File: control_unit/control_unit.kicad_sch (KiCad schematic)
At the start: 52 parts, among them J1 Conn_01x02_Pin, J2 Conn_01x02_Pin, J3 Conn_01x04_Pin, J4 Conn_01x04_Pin, J5 BLDC1, J6 Conn_01x04_Pin, J7 BLDC2, J8 BLDC3, J9 BLDC4, Q2 2N7002, U4 BNO055

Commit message: DCDCコンバーター設計開始
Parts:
- removed C10, C3, C7, C8, C9: 22uF, Capacitor_SMD:C_1206_3216Metric, symbol Device:C
- removed C2, C4: 0.1u, symbol Device:C
- removed C5: 1u, symbol Device:C
- removed J2: Conn_01x02_Pin, Connector_PinHeader_2.54mm:PinHeader_1x02_P2.54mm_Vertical, symbol Connector:Conn_01x02_Pin
- removed J3, J6: Conn_01x04_Pin, Connector_PinHeader_2.54mm:PinHeader_1x04_P2.54mm_Vertical, symbol Connector:Conn_01x04_Pin
- removed Q3: ~, Package_TO_SOT_SMD:TO-252-2, symbol basic_parts:MTP7D0N6RJ3
- removed R14: 100k, symbol Device:R
- removed U14: ~, ProLib_pcs_2025-03-30:VSON-10_L3.0-W3.0-P0.50-BR-EP, symbol basic_parts:TPS40303DRCT
- removed U4: BNO055, Package_LGA:LGA-28_5.2x3.8mm_P0.5mm, symbol Sensor_Motion:BNO055
- added Cbst, Cc1, Cc2, Cc3, Css, Cvcc: C, symbol Device:C
- added Cin1, Cin2, Cin3, Cin4, Cin5, Cout1, Cout2, Cout3, Cout4, Cout5, Cout6: 22u, symbol Device:C
- added L2: 6.8uH, symbol Device:L
- added Q2: ~, Package_TO_SOT_SMD:TO-252-2, symbol basic_parts:MTP7D0N6RJ3
- added Q4: 2N7002, Package_TO_SOT_SMD:SOT-23, symbol Transistor_FET:2N7002
- added Rc1, Rc2, Rfb1, Rfb2, Rpg, Rt: R, symbol Device:R
- added Ruv1: 75k, symbol Device:R
- added Ruv2: 12k, symbol Device:R
- added U5: ~, basic_parts:VQFN-20_L4.5-W3.5-P0.50-BL-EP, symbol basic_parts:LM25145RGYR
- C1: value 0.33u -> C
- renumbered Q2 to Q3
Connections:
- net +5V: now also U10.2 (VDD), U11.2 (VDD), U12.2 (VDD), U13.2 (VDD)
- net GND: now also Cin1.2, Cin2.2, Cin3.2, Cin4.2, Cin5.2, Cout1.2, Cout2.2, Cout3.2, Cout4.2, Cout5.2, Cout6.2, Css.1, Cvcc.2, Q2.3 (S), Q4.2 (S), Rfb2.1, Rt.1, Ruv2.2, U5.12 (PGND), U5.15 (EP), U5.16 (NC), U5.21 (EP), U5.6 (AGND); no longer Q1.3 (S)
- net LowBeam: now also U2.31 (GPIO6); no longer U2.21 (GPIO9)
- net PGOOD: now also Rpg.1, U5.10 (PGOOD)
- net SERVO_LOGIC: no longer U10.2 (VDD), U11.2 (VDD), U12.2 (VDD), U13.2 (VDD)
- net at D3.1 (K), D5.1 (K), Q3.3 (D): no longer D4.1 (K), D6.1 (K)
- net +24V: now reaches C1.1
- net +24V: now also Q1.2 (D), Cin1.1, Cin2.1, Cin3.1, Cin4.1, Cin5.1, Ruv1.1, U5.20 (VIN)
- net at Q1.1 (G): now also U5.18 (HO)
- new net: Cbst.2, L2.1, Q1.3 (S), Q2.2 (D), U5.19 (SW)
- new net: D4.1 (K), D6.1 (K), Q4.3 (D)
- new net: Cc3.1, Rc2.1
- new net: Cc1.1, Rc1.1
- new net: Cc2.1, Cc3.2, Rc1.2, Rfb1.1, Rfb2.2, U5.5 (FB)
- new net: Cc1.2, Cc2.2, U5.4 (COMP)
- new net: Ruv1.2, Ruv2.1, U5.1 (EN/UVLO)
- new net: Q2.1 (G), U5.13 (LO)
- new net: Cbst.1, U5.17 (BST)
- new net: Css.2, U5.3 (SS/TRK)
- new net: Rt.2, U5.2 (RT)
- new net +5.1V: Cout1.1, Cout2.1, Cout3.1, Cout4.1, Cout5.1, Cout6.1, L2.2, Rc2.2, Rfb1.2
- new net +7.5V: Cvcc.1, Rpg.2, U5.14 (VCC)
- new net IR: Q4.1 (G), U2.21 (GPIO9)
- no-connect marks 4 -> 6
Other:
- note added: "DC DC converter"
- note added: "High Power LED"
- note added: "Low Power LED"
- note removed: "CANでモーター制御基板と通信をとる"
- note removed: "Calibration time 1.9ms Soft start time = 20ms tss=CV/I I=10uA V=0.6A"
- title: (none) -> UMIUSI2_control_unit
- moved on the sheet: D1, D3, D4, D5, D6, D7, D8, D9, J1, J4, J5, J7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

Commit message: ファイル追加
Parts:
- added Rilim: 270, symbol Device:R
- C1, Cbst, Css: value C -> 0.1u
- Cvcc: value C -> 2.2u
- Rpg: value R -> 51k
- Rt: value R -> 33k
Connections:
- net at Cbst.2, L2.1, Q1.3 (S)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: now also Rilim.2
- net at U5.11 (ILIM): now also Rilim.1
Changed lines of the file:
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@@
 	(text "DC DC converter"
 		(exclude_from_sim no)
-		(at 49.022 16.002 0)
+		(at 47.244 15.494 0)
 		(effects
 			(font
@@
 	)
 	(junction
+		(at 92.71 46.99)
+		(diameter 0)
+		(color 0 0 0 0)
+	)
+	(junction
 		(at 134.62 54.61)
 		(diameter 0)
@@
 	(wire
 		(pts
+			(xy 82.55 58.42) (xy 92.71 58.42)
+		)
+		(stroke
+			(width 0)
+			(type default)
+		)
+	)
+	(wire
+		(pts
 			(xy 248.92 139.7) (xy 257.81 139.7)
 		)
@@
 	(wire
 		(pts
-			(xy 82.55 55.88) (xy 90.17 55.88)
+			(xy 82.55 55.88) (xy 87.63 55.88)
 		)
 		(stroke
@@
 	(wire
 		(pts
+			(xy 92.71 50.8) (xy 92.71 46.99)
+		)
+		(stroke
+			(width 0)
+			(type default)
+		)
+	)
+	(wire
+		(pts
 			(xy 147.32 46.99) (xy 153.67 46.99)
 		)
@@
 	(wire
 		(pts
-			(xy 68.58 72.39) (xy 68.58 66.04)
+			(xy 68.58 71.12) (xy 68.58 66.04)
 		)
 		(stroke
@@
 	(wire
 		(pts
-			(xy 90.17 55.88) (xy 90.17 57.15)
-		)
-		(stroke
-			(width 0)
-			(type default)
-		)
-	)
-	(wire
-		(pts
 			(xy 182.88 111.76) (xy 182.88 119.38)
 		)
@@
 	(symbol
 		(lib_id "power:GND")
-		(at 90.17 57.15 0)
+		(at 87.63 55.88 0)
 		(unit 1)
 		(exclude_from_sim no)
@@
 		(on_board yes)
 		(dnp no)
-		(fields_autoplaced yes)
 		(property "Reference" "#PWR016"
-			(at 90.17 63.5 0)
+			(at 87.63 62.23 0)
 			(effects
 				(font
@@
 		)
 		(property "Value" "GND"
-			(at 90.17 62.23 0)
+			(at 87.63 56.134 0)
 			(effects
 				(font
@@
 		)
 		(property "Footprint" ""
-			(at 90.17 57.15 0)
+			(at 87.63 55.88 0)
 			(effects
 				(font
@@
 		)
 		(property "Datasheet" ""
-			(at 90.17 57.15 0)
+			(at 87.63 55.88 0)
 			(effects
 				(font
@@
 		)
 		(property "Description" "Power symbol creates a global label with name \"GND\" , ground"
-			(at 90.17 57.15 0)
+			(at 87.63 55.88 0)
 			(effects
 				(font
@@
 			)
 		)
-		(property "Value" "C"
+		(property "Value" "0.1u"
 			(at 91.44 22.86 90)
 			(effects
@@
 	(symbol
 		(lib_id "power:GND")
-		(at 68.58 72.39 0)
+		(at 68.58 71.12 0)
 		(unit 1)
 		(exclude_from_sim no)
@@
 		(fields_autoplaced yes)
 		(property "Reference" "#PWR018"
-			(at 68.58 78.74 0)
+			(at 68.58 77.47 0)
 			(effects
 				(font
@@
 		)
 		(property "Value" "GND"
-			(at 68.58 77.47 0)
+			(at 68.58 76.2 0)
 			(effects
 				(font
@@
 		)
 		(property "Footprint" ""
-			(at 68.58 72.39 0)
+			(at 68.58 71.12 0)
 			(effects
 				(font
@@
 		)
 		(property "Datasheet" ""
-			(at 68.58 72.39 0)
+			(at 68.58 71.12 0)
 			(effects
 				(font
@@
 		)
 		(property "Description" "Power symbol creates a global label with name \"GND\" , ground"
-			(at 68.58 72.39 0)
+			(at 68.58 71.12 0)
 			(effects
 				(font
@@
 	)
 	(symbol
+		(lib_id "Device:R")
+		(at 92.71 54.61 0)
+		(mirror x)
+		(unit 1)
+		(exclude_from_sim no)
+		(in_bom yes)
+		(on_board yes)
+		(dnp no)
+		(property "Reference" "Rilim"
+			(at 95.758 54.864 0)
+			(effects
+				(font
+					(size 1.27 1.27)
+				)
+			)
+		)
+		(property "Value" "270"
+			(at 95.758 56.896 0)
+			(effects
+				(font
+					(size 1.27 1.27)
+				)
+			)
+		)
+		(property "Footprint" ""
+			(at 90.932 54.61 90)
+			(effects
+				(font
+					(size 1.27 1.27)
+				)
+				(hide yes)
+			)
+		)
+		(property "Datasheet" "~"
+			(at 92.71 54.61 0)
+			(effects
+				(font
+					(size 1.27 1.27)
+				)
+				(hide yes)
+			)
+		)
+		(property "Description" "Resistor"
+			(at 92.71 54.61 0)
+			(effects
+				(font
+					(size 1.27 1.27)
+				)
+				(hide yes)
+			)
+		)
+		(pin "1"
+		)
+		(pin "2"
+		)
+		(instances
+			(project ""
+				(path "/37a62e38-d605-4440-86b8-fb3d0940d64a"
+					(reference "Rilim")
+					(unit 1)
+				)
+			)
+		)
+	)
+	(symbol
 		(lib_id "Device:C")
 		(at 153.67 50.8 0)
@@
 			)
 		)
-		(property "Value" "C"
+		(property "Value" "2.2u"
 			(at 88.9 68.5799 0)
 			(effects
@@
 			)
 		)
-		(property "Value" "C"
+		(property "Value" "0.1u"
 			(at 88.9 38.1 90)
 			(effects
@@
 			)
 		)
-		(property "Value" "C"
+		(property "Value" "0.1u"
 			(at 50.292 41.656 90)
 			(effects
@@
 			)
 		)
-		(property "Value" "R"
+		(property "Value" "51k"
 			(at 60.96 67.31 90)
 			(effects
@@
 		(on_board yes)
 		(dnp no)
-		(fields_autoplaced yes)
 		(property "Reference" "Rt"
-			(at 49.53 31.75 90)
+			(at 46.736 34.29 90)
 			(effects
 				(font
@@
 			)
 		)
-		(property "Value" "R"
-			(at 49.53 34.29 90)
+		(property "Value" "33k"
+			(at 46.736 36.322 90)
 			(effects
 				(font

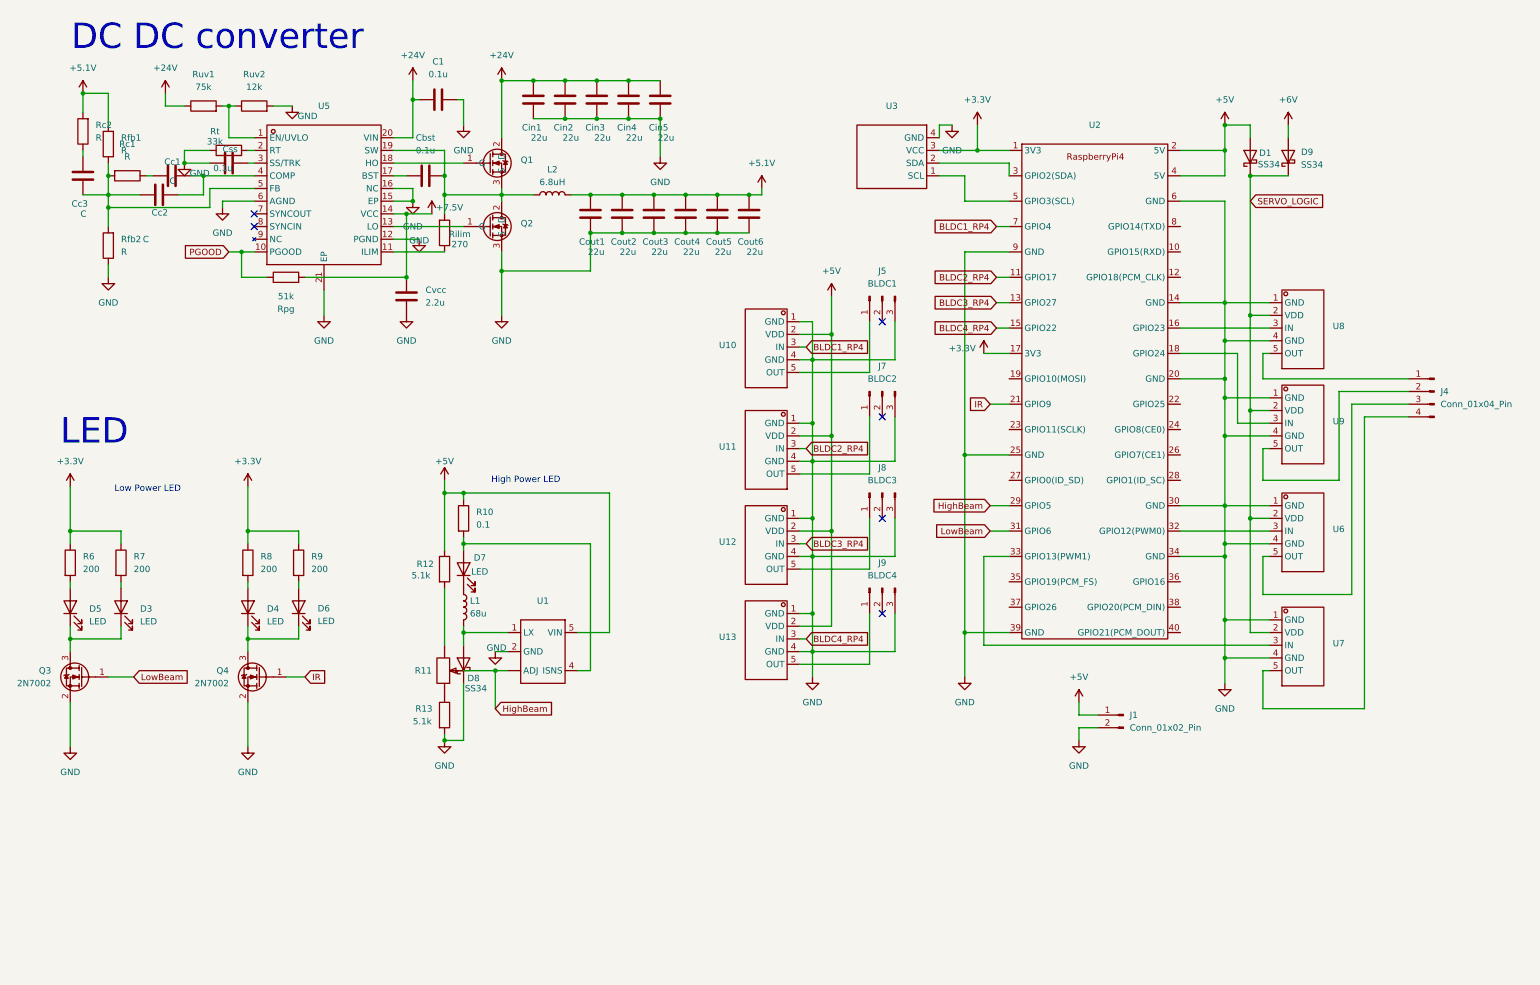
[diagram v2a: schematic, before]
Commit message: DCDCコンバーター設計完了
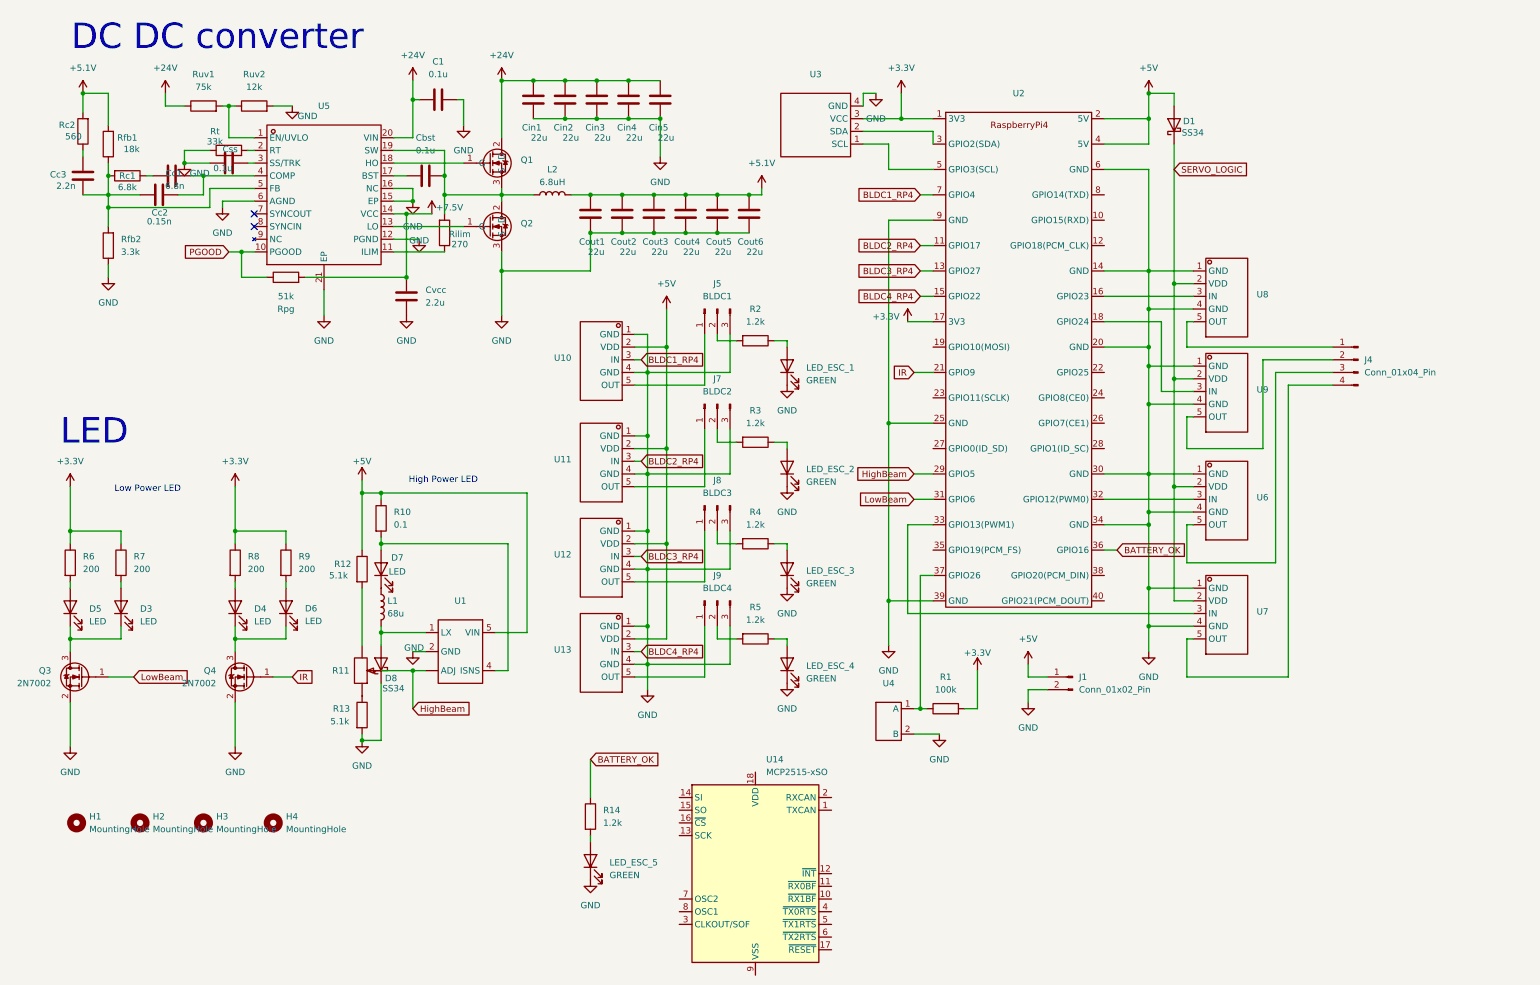
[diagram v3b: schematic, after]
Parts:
- removed D9: SS34, Diode_SMD:D_SMA, symbol Diode:SS34
- added H1, H2, H3, H4: MountingHole, MountingHole:MountingHole_3.2mm_M3, symbol Mechanical:MountingHole
- added LED_ESC_1, LED_ESC_2, LED_ESC_3, LED_ESC_4, LED_ESC_5: GREEN, symbol Device:LED
- added R1: 100k, symbol Device:R
- added R14, R2, R3, R4, R5: 1.2k, symbol Device:R
- added U14: MCP2515-xSO, Package_SO:SOIC-18W_7.5x11.6mm_P1.27mm, symbol Interface_CAN_LIN:MCP2515-xSO
- added U4: ~, basic_parts:wetness sensor, symbol basic_parts:wetness_sensor
- Cc1: value C -> 6.8n
- Cc2: value C -> 0.15n
- Cc3: value C -> 2.2n
- Rc1: value R -> 6.8k
- Rc2: value R -> 560
- Rfb1: value R -> 18k
- Rfb2: value R -> 3.3k
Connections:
- net +3.3V: now also R1.2
- net GND: now also LED_ESC_1.1 (K), LED_ESC_2.1 (K), LED_ESC_3.1 (K), LED_ESC_4.1 (K), LED_ESC_5.1 (K), U4.2 (B)
- net at J8.2 (Pin_2): now also R4.2
- net at J9.2 (Pin_2): now also R5.2
- net BATTERY_OK: now reaches U2.36 (GPIO16)
- net BATTERY_OK: now also R14.1
- net at U2.37 (GPIO26): now also R1.1, U4.1 (A)
- net at J5.2 (Pin_2): now also R2.2
- net at J7.2 (Pin_2): now also R3.2
- new net: LED_ESC_1.2 (A), R2.1
- new net: LED_ESC_2.2 (A), R3.1
- new net: LED_ESC_4.2 (A), R5.1
- new net: LED_ESC_3.2 (A), R4.1
- new net: LED_ESC_5.2 (A), R14.2
- no-connect marks 6 -> 2
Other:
- moved on the sheet: D1, D4, D6, D7, D8, J1, J4, J5, J7, J8, J9, L1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

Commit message: 入力コンデンサ、出力コンデンサを直した
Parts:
- removed Cout5, Cout6: 22u, symbol Device:C
- added Cin10, Cin11, Cin12, Cin13, Cin14, Cin15, Cin16, Cin17, Cin6, Cin7, Cin8, Cin9: 10u, Capacitor_SMD:C_1210_3225Metric_Pad1.33x2.70mm_HandSolder, symbol Device:C
- Cc1: value 6.8n -> 4.7n
- Cin1, Cin2, Cin3, Cin4, Cin5: value 22u -> 10u; footprint (none) -> Capacitor_SMD:C_1210_3225Metric_Pad1.33x2.70mm_HandSolder
- Cout1, Cout2, Cout3, Cout4: value 22u -> 47u; footprint (none) -> Capacitor_SMD:C_1210_3225Metric
- L2: value 6.8uH -> 10u; LCSC C149517 -> C149518
- Rc1: value 6.8k -> 5.6k
- Rc2: value 560 -> 600
- Rilim: value 270 -> 180
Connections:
- net GND is gone; now on net +24V: C1.2, Cin1.2, Cin2.2, Cin3.2, Cin4.2, Cin5.2, Cout1.2, Cout2.2, Cout3.2, Cout4.2, Css.1, Cvcc.2, D8.1 (K), J1.2 (Pin_2), J5.3 (Pin_3), J7.3 (Pin_3), J8.3 (Pin_3), J9.3 (Pin_3), LED_ESC_1.1 (K), LED_ESC_2.1 (K), LED_ESC_3.1 (K), LED_ESC_4.1 (K), LED_ESC_5.1 (K), Q2.3 (S), Q3.2 (S), Q4.2 (S), R13.2, Rfb2.1, Rt.1, Ruv2.2, U1.2 (GND), U10.1 (GND), U10.4 (GND), U11.1 (GND), U11.4 (GND), U12.1 (GND), U12.4 (GND), U13.1 (GND), U13.4 (GND), U2.14 (GND), U2.20 (GND), U2.25 (GND), U2.30 (GND), U2.34 (GND), U2.39 (GND), U2.6 (GND), U2.9 (GND), U3.4 (GND), U4.2 (B), U5.12 (PGND), U5.15 (EP), U5.16 (NC), U5.21 (EP), U5.6 (AGND), U6.1 (GND), U6.4 (GND), U7.1 (GND), U7.4 (GND), U8.1 (GND), U8.4 (GND), U9.1 (GND), U9.4 (GND)
- net +24V: now also U5.8 (SYNCIN), Cin10.1, Cin10.2, Cin11.1, Cin11.2, Cin12.1, Cin12.2, Cin13.1, Cin13.2, Cin14.1, Cin14.2, Cin15.1, Cin15.2, Cin16.1, Cin16.2, Cin17.1, Cin17.2, Cin6.1, Cin6.2, Cin7.1, Cin7.2, Cin8.1, Cin8.2, Cin9.1, Cin9.2
- no-connect marks 2 -> 1
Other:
- moved on the sheet: C1, Cbst, Cc1, Cc2, Cc3, Cin1, Cout1, Css, Cvcc, D1, D3, D4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
